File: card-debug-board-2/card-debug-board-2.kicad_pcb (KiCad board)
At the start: 2 copper layers, 36 x 52 mm, 30 parts, among them J1 2-1734592-0, J2 Conn_01x05, J5 0676430910, J6 629105150521, SW1 PCM13SMTR, SW2 B3F-1000, SW3 CFS-0103TB, SW4 CFS-0103TB, U1 MIC5205-3.3YM5

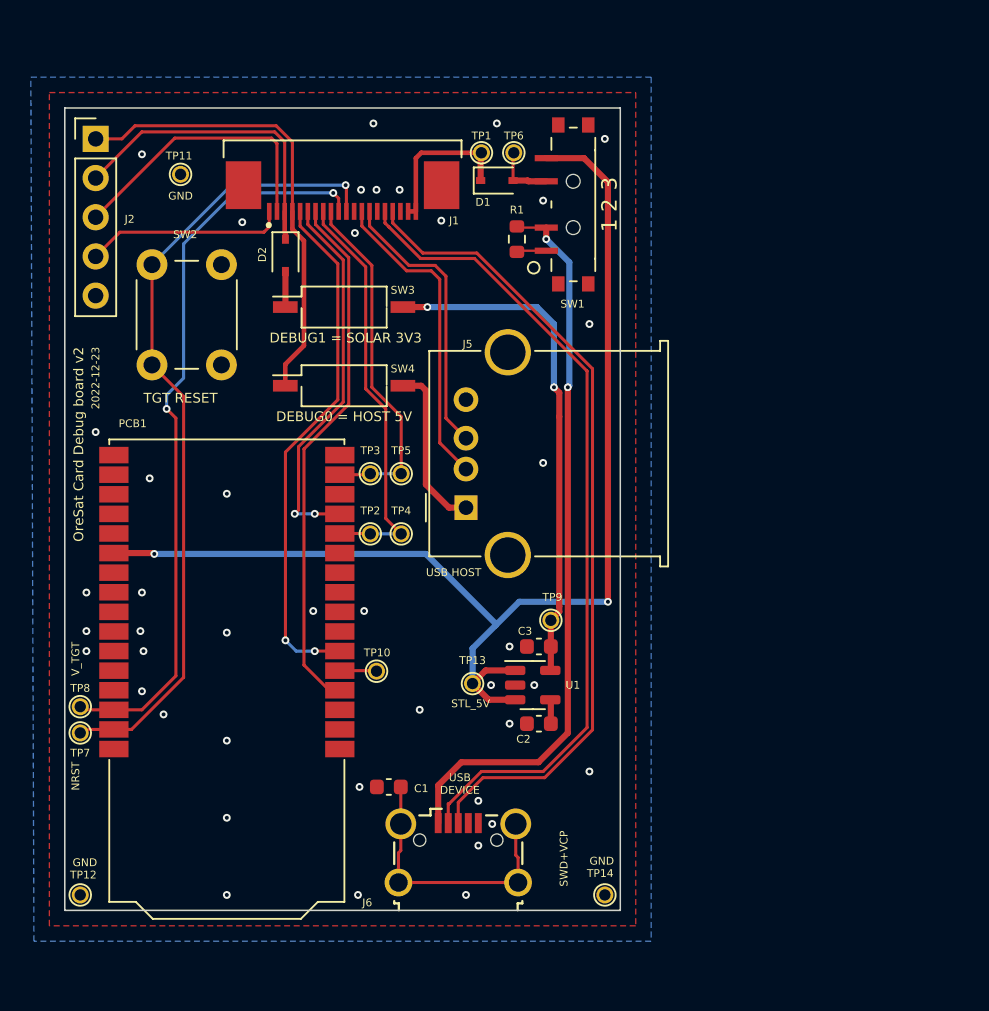
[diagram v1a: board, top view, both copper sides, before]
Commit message: Card Debug Board v3
new switch & layout (tracing not finished).
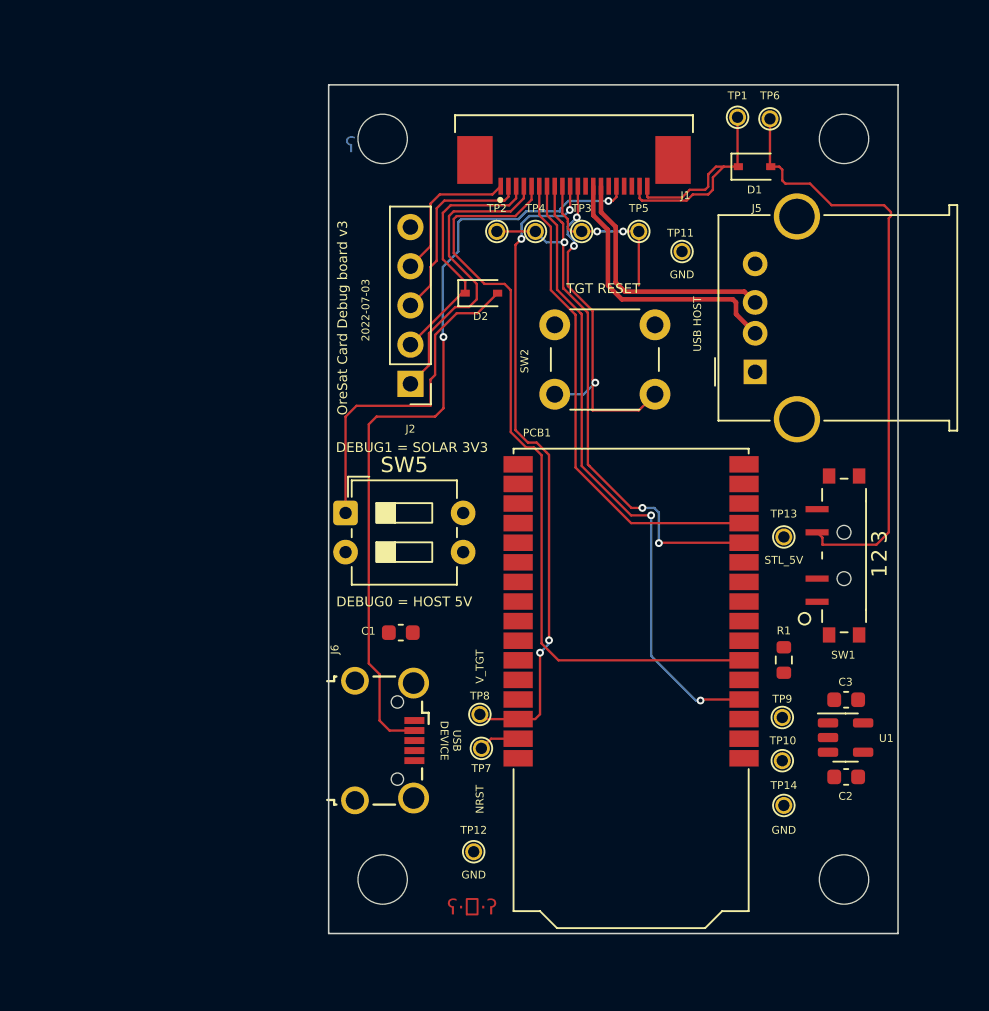
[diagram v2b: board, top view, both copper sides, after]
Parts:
- removed SW3, SW4: CFS-0103TB, Button_Switch_SMD:SW_DIP_SPSTx01_Slide_Copal_CHS-01B_W7.62mm_P1.27mm
- added REF**: MountingHole_3.2mm_M3, MountingHole:MountingHole_3.2mm_M3, F.Cu at (176.5, 50.0)
- added REF**: MountingHole_3.2mm_M3, MountingHole:MountingHole_3.2mm_M3, F.Cu at (146.6, 98.0)
- added REF**: MountingHole_3.2mm_M3, MountingHole:MountingHole_3.2mm_M3, F.Cu at (176.5, 98.0)
- added REF**: MountingHole_3.2mm_M3, MountingHole:MountingHole_3.2mm_M3, F.Cu at (146.6, 50.0)
- added SW5: 210-2LPS, Button_Switch_THT:SW_DIP_SPSTx02_Slide_6.7x6.64mm_W7.62mm_P2.54mm_LowProfile, F.Cu at (144.2, 74.2)
- J1: value 2-1734592-0 -> 2-1734592-0
- moved TP11 32.9 mm to (166.0, 57.3)
- moved R1 32.3 mm to (172.6, 83.8)
- moved SW1 28.7 mm to (176.5, 77.0)
- moved TP10 26.9 mm to (172.5, 90.3)
- moved PCB1 26.2 mm to (162.7, 100.0)
- moved TP7 26.0 mm to (153.0, 89.5)
- moved TP8 25.9 mm to (152.9, 87.3)
- moved J2 25.8 mm to (148.4, 65.9), turned to 180 degrees
- moved TP12 25.7 mm to (152.5, 96.2)
- moved TP13 22.3 mm to (172.6, 75.8)
- moved TP5 22.0 mm to (163.2, 56.0)
- moved SW2 21.9 mm to (157.8, 62.0), turned to 0 degrees
- moved TP4 21.4 mm to (156.5, 56.0)
- moved TP2 21.2 mm to (154.0, 56.0)
- moved TP3 20.8 mm to (159.5, 56.0)
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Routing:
- net +5V: track 77.1 -> 0.00 mm, vias 2 -> 0
- net Net-(J1-DEVICE-D+): track 53.0 -> 0.00 mm
- net Net-(J6-VBUS): track 47.6 -> 0.00 mm, vias 2 -> 0
- net Net-(D1-A): track 4.00 -> 38.9 mm
- net +3.3V: track 33.1 -> 0.00 mm, vias 2 -> 0
- net Net-(J1-NRST): track 52.2 -> 26.0 mm, vias 1 -> 3
- net Net-(D2-A): track 2.30 -> 21.9 mm
- net Net-(J6-Shield): track 17.9 -> 0.00 mm
- net Net-(J1-SWO): track 34.0 -> 50.9 mm, vias 2 -> 0
- net Net-(J1-CARD-RX): track 22.9 -> 10.9 mm, vias 0 -> 2
- net Net-(J5-VBUS): track 10.9 -> 0.00 mm
- net Net-(J1-CARD-TX): track 27.0 -> 37.1 mm, vias 0 -> 3
- net /DEBUG0/5VUSBHOST: track 30.1 -> 20.0 mm
- net Net-(D1-K): track 10.2 -> 18.8 mm
- net Net-(J1-SWCLK): track 24.8 -> 31.6 mm, vias 2 -> 0
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- removed copper zone on B.Cu, net GND
- removed copper zone on F.Cu, net GND
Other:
- board size 36 x 52 mm -> 36.9 x 55 mm
- board text added: "2022-07-03"
- board text added: "OreSat Card Debug board v3"
- board text added: "ʕ·ᴥ·ʔ﻿"
- board text removed: "2022-12-23"
- board text removed: "OreSat Card Debug board v2"
- board text removed: "SWD+VCP"

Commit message: Debug Board V3
DONE(??????)
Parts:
- removed the REF** at (176.5, 50.0)
- removed the REF** at (146.6, 98.0)
- removed the REF** at (176.5, 98.0)
- removed the REF** at (146.6, 50.0)
- added REF**: MountingHole_3.2mm_M3, MountingHole:MountingHole_3.2mm_M3, F.Cu at (176.6, 98.0)
- added REF**: MountingHole_3.2mm_M3, MountingHole:MountingHole_3.2mm_M3, F.Cu at (146.6, 98.0)
- added REF**: MountingHole_3.2mm_M3, MountingHole:MountingHole_3.2mm_M3, F.Cu at (176.6, 50.0)
- added REF**: MountingHole_3.2mm_M3, MountingHole:MountingHole_3.2mm_M3, F.Cu at (146.6, 50.0)
- moved J6 41.8 mm to (176.2, 59.3), turned to 90 degrees
- moved SW2 32.6 mm to (146.2, 92.5), turned to 90 degrees
- moved C1 28.4 mm to (170.0, 64.3), turned to 90 degrees
- moved R1 22.8 mm to (170.0, 61.1)
- moved J5 19.6 mm to (152.5, 72.2), turned to -90 degrees
- moved SW5 19.2 mm to (159.3, 62.3)
- moved TP9 19.1 mm to (168.2, 68.9)
- moved TP6 17.5 mm to (172.8, 66.2)
- moved D1 16.2 mm to (171.8, 67.9)
- moved TP13 9.72 mm to (174.6, 66.3)
- moved TP5 8.46 mm to (155.1, 58.3)
- moved TP3 6.97 mm to (152.9, 58.3)
- moved TP1 6.70 mm to (166.9, 54.7)
- moved C2 6.58 mm to (176.3, 84.8)
- moved C3 6.53 mm to (176.4, 79.8)
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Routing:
- net Net-(J1-NRST): track 26.0 -> 64.7 mm, vias 3 -> 4
- net +5V: track 0.00 -> 35.1 mm, vias 0 -> 2
- net Net-(J1-DEVICE-D-): track 51.6 -> 16.9 mm, vias 2 -> 0
- net Net-(D1-A): track 38.9 -> 5.11 mm
- net Net-(J1-SWO): track 50.9 -> 77.9 mm, vias 0 -> 2
- net Net-(J1-CARD-RX): track 10.9 -> 36.2 mm, vias 2 -> 1
- net Net-(J6-VBUS): track 0.00 -> 22.2 mm
- net Net-(R1-Pad2): track 0.00 -> 21.6 mm
- net Net-(J5-VBUS): track 0.00 -> 18.7 mm, vias 0 -> 2
- net Net-(D2-A): track 21.9 -> 4.77 mm, vias 0 -> 1
- net Net-(J1-DEVICE-D+): track 0.00 -> 15.9 mm
- net GND: track 0.00 -> 12.7 mm, vias 0 -> 34
- net Net-(J1-HOST-D+): track 16.2 -> 28.0 mm
- net /DEBUG0/5VUSBHOST: track 20.0 -> 30.3 mm, vias 0 -> 3
- net Net-(D1-K): track 18.8 -> 28.4 mm, vias 0 -> 4
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- added copper zone on B.Cu, net GND
- added copper zone on F.Cu, net GND
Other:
- board text removed: "STL_5V"

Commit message: restore v2 card debug board files
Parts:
- removed REF** (x4): MountingHole_3.2mm_M3, MountingHole:MountingHole_3.2mm_M3
- removed SW5: 210-2LPS, Button_Switch_THT:SW_DIP_SPSTx02_Slide_6.7x6.64mm_W7.62mm_P2.54mm_LowProfile
- added SW3: CFS-0103TB, Button_Switch_SMD:SW_DIP_SPSTx01_Slide_Copal_CHS-01B_W7.62mm_P1.27mm, F.Cu at (144.1, 60.9)
- added SW4: CFS-0103TB, Button_Switch_SMD:SW_DIP_SPSTx01_Slide_Copal_CHS-01B_W7.62mm_P1.27mm, F.Cu at (144.1, 66.0)
- J1: value 2-1734592-0 -> 2-1734592-0
- moved J6 44.5 mm to (151.5, 96.2), turned to 0 degrees
- moved C1 36.0 mm to (147.0, 92.0), turned to 180 degrees
- moved SW2 35.9 mm to (136.2, 58.1), turned to -90 degrees
- moved TP10 30.6 mm to (146.2, 84.5)
- moved TP13 29.2 mm to (152.4, 85.3)
- moved TP11 28.7 mm to (133.5, 52.3)
- moved PCB1 28.1 mm to (136.5, 99.5)
- moved TP7 27.7 mm to (127.0, 88.5)
- moved TP8 27.6 mm to (127.0, 86.8)
- moved TP12 25.7 mm to (127.0, 99.0)
- moved SW1 24.6 mm to (158.9, 54.2)
- moved J2 24.4 mm to (128.0, 50.0), turned to 0 degrees
- moved D1 23.4 mm to (154.0, 52.7)
- moved TP6 23.3 mm to (155.1, 50.9)
- moved U1 20.2 mm to (156.3, 85.4)
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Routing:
- net Net-(J1-SWO): track 77.9 -> 34.0 mm
- net +5V: track 35.1 -> 77.1 mm
- net Net-(J1-DEVICE-D+): track 15.9 -> 53.0 mm
- net Net-(J1-DEVICE-D-): track 16.9 -> 53.2 mm
- net Net-(J6-VBUS): track 22.2 -> 47.6 mm, vias 0 -> 2
- net +3.3V: track 9.47 -> 33.1 mm, vias 0 -> 2
- net Net-(R1-Pad2): track 21.6 -> 1.94 mm
- net Net-(D1-K): track 28.4 -> 10.2 mm, vias 4 -> 0
- net Net-(J1-CARD-TX): track 42.6 -> 27.0 mm, vias 2 -> 0
- net Net-(J1-CARD-RX): track 36.2 -> 22.9 mm, vias 1 -> 0
- net GND: track 12.7 -> 0.00 mm, vias 34 -> 42
- net Net-(J6-Shield): track 5.36 -> 17.9 mm
- net Net-(J1-NRST): track 64.7 -> 52.2 mm, vias 4 -> 1
- net Net-(J1-HOST-D+): track 28.0 -> 18.3 mm
- net Net-(J5-VBUS): track 18.7 -> 10.9 mm, vias 2 -> 0
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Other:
- board size 36.9 x 55 mm -> 36 x 52 mm
- board text added: "2022-12-23"
- board text added: "OreSat Card Debug board v2"
- board text added: "STL_5V"
- board text added: "SWD+VCP"
- board text removed: "2022-07-03"
- board text removed: "OreSat Card Debug board v3"
- board text removed: "ʕ·ᴥ·ʔ﻿"
